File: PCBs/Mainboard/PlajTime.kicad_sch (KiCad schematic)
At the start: 7 parts, among them IC5 TXS0102DQMR, J10 2328702-4, J6 6pin_conn, J7 Phototransistor, J9 side button

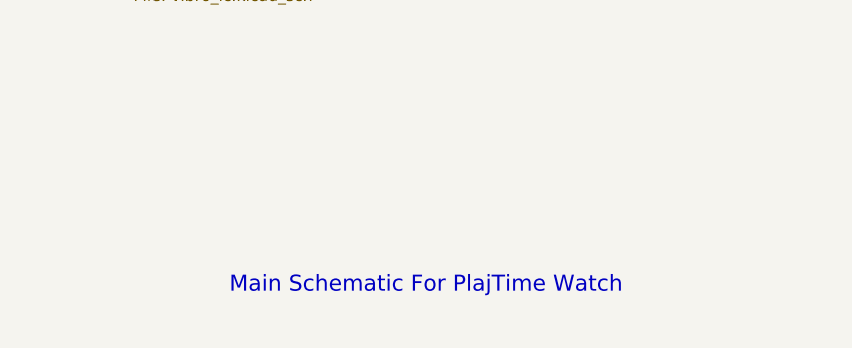
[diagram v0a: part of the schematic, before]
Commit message: Add progress report for 31.1.2025 Update relevant source files
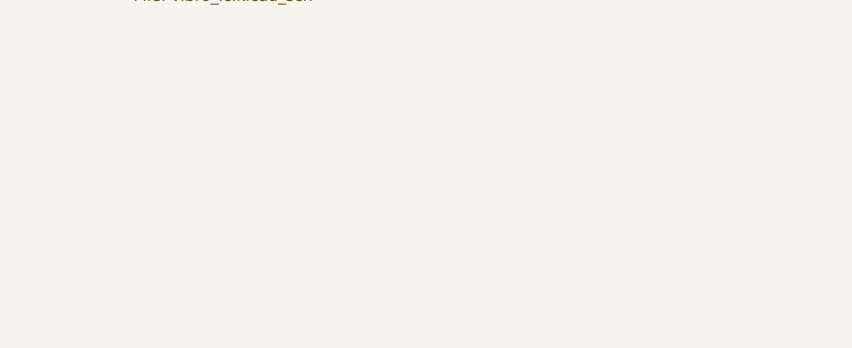
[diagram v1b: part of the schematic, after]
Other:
- note removed: "Main Schematic For PlajTime Watch"
- title: (none) -> Main
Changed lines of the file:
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@@
 	(generator_version "8.0")
 	(paper "A4")
+	(title_block
+		(title "Main")
+	)
 	(junction
 		(at 16.51 105.41)
@@
 		)
 	)
-	(text "Main Schematic For PlajTime Watch"
-		(exclude_from_sim no)
-		(at 211.582 189.738 0)
-		(effects
-			(font
-				(size 1.778 1.778)
-			)
-		)
-	)
 	(label "VSYS"
 		(at 214.63 152.4 180)
-		(fields_autoplaced yes)
 		(effects
 			(font
@@
 	(label "VSYS"
 		(at 109.22 60.96 180)
-		(fields_autoplaced yes)
 		(effects
 			(font
@@
 	(label "SCL_1V8"
 		(at 245.11 102.87 0)
-		(fields_autoplaced yes)
 		(effects
 			(font
@@
 	(label "OXY_INT"
 		(at 167.64 76.2 270)
-		(fields_autoplaced yes)
 		(effects
 			(font
@@
 	(label "IMU_INT"
 		(at 157.48 76.2 270)
-		(fields_autoplaced yes)
 		(effects
 			(font
@@
 	(label "NFC_INT"
 		(at 162.56 76.2 270)
-		(fields_autoplaced yes)
 		(effects
 			(font
@@
 	(label "VSYS"
 		(at 171.45 60.96 180)
-		(fields_autoplaced yes)
 		(effects
 			(font
@@
 	(label "DP_RES"
 		(at 160.02 76.2 270)
-		(fields_autoplaced yes)
 		(effects
 			(font
@@
 	(label "IN+"
 		(at 41.91 87.63 270)
-		(fields_autoplaced yes)
 		(effects
 			(font
@@
 	(label "VIC_INT"
 		(at 184.15 88.9 90)
-		(fields_autoplaced yes)
 		(effects
 			(font
@@
 	(label "DP_RES"
 		(at 114.3 67.31 180)
-		(fields_autoplaced yes)
 		(effects
 			(font
@@
 	(label "IN+"
 		(at 171.45 63.5 180)
-		(fields_autoplaced yes)
 		(effects
 			(font
@@
 	(label "PIC_INT"
 		(at 167.64 72.39 0)
-		(fields_autoplaced yes)
 		(effects
 			(font
@@
 	(label "1V8_EN"
 		(at 165.1 76.2 270)
-		(fields_autoplaced yes)
 		(effects
 			(font
@@
 	(label "SDA_1V8"
 		(at 245.11 100.33 0)
-		(fields_autoplaced yes)
 		(effects
 			(font
@@
 	(label "LVL_SHIFT_EN"
 		(at 212.09 93.98 90)
-		(fields_autoplaced yes)
-		(effects
-			(font
+		(effects
+			(font
